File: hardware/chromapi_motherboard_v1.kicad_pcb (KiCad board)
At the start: 4 copper layers, 139 parts, among them J1 Battery Input, J10 Top Left Switch, J11 Top Right Switch, J12 Bottom Left Switch, J13 Bottom Right Switch, J14 RPI_Connector, J2 Power Switch, J3 USB_C_Receptacle_USB2.0_14P, J4 Conn_ST_STDC14, J5 Conn_TopLeft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

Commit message: rm cached
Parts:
- H2, H3, H4, H5: footprint MountingHole:MountingHole_2.7mm_M2.5_ISO14580_Pad_TopBottom -> MountingHole:MountingHole_2.7mm_M2.5_Pad_Via
- U2: footprint Package_SO:VSSOP-10_3x3mm_P0.5mm -> Package_SO:TSSOP-10_3x3mm_P0.5mm
- moved TP4 59.8 mm to (146.0, 122.0)
- moved R24 52.5 mm to (148.5, 121.3), turned to 90 degrees
- moved TP3 52.1 mm to (151.5, 122.0)
- moved D7 48.8 mm to (148.5, 124.2), turned to 90 degrees
- moved R23 45.2 mm to (154.0, 121.5), turned to 90 degrees
- moved TP2 45.2 mm to (157.5, 122.0)
- moved D6 41.8 mm to (154.0, 124.4), turned to 90 degrees
- moved R22 37.6 mm to (160.0, 121.6), turned to 90 degrees
- moved J5 37.4 mm to (186.0, 122.4), turned to 0 degrees
- moved D5 34.7 mm to (160.0, 124.5), turned to 90 degrees
- moved J7 31.2 mm to (186.0, 116.4), turned to 0 degrees
- moved J6 30.5 mm to (175.0, 122.5), turned to 0 degrees
- moved TP1 24.3 mm to (205.0, 121.5)
- moved J8 22.2 mm to (175.0, 116.4), turned to 0 degrees
- moved C5 19.1 mm to (191.5, 108.3)
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
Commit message: First routing draft
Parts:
- moved FID3 54.0 mm to (192.7, 80.7)
- moved FID2 32.2 mm to (150.0, 107.3)
- moved C36 17.7 mm to (132.2, 116.5)
- moved C37 17.7 mm to (140.7, 116.5)
- moved J11 17.5 mm to (141.5, 122.5)
- moved R33 17.5 mm to (133.5, 118.0)
- moved R34 17.5 mm to (142.0, 118.0)
- moved J10 17.5 mm to (133.0, 122.5)
- moved J12 16.5 mm to (116.0, 122.5)
- moved J13 16.5 mm to (124.5, 122.5)
- moved C39 16.5 mm to (123.7, 116.5)
- moved R35 16.5 mm to (116.5, 118.0)
- moved R36 16.5 mm to (125.0, 118.0)
- moved C38 16.3 mm to (115.2, 116.5)
- moved J8 11.1 mm to (186.1, 116.4)
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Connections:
- J14 pad 36: unconnected-(J14-Pin_36-Pad36) -> /Raspberry Pi Interface/NRST
- J14 pad 37: /Raspberry Pi Interface/NRST -> unconnected-(J14-Pin_37-Pad37)
- J2 pad 1: /Power Supply & Charge/B+ -> /Power Supply & Charge/V_BATT
- J2 pad 2: /Power Supply & Charge/V_BATT -> /Power Supply & Charge/B+
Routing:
- net +3.3V: track 0.00 -> 266.6 mm, vias 0 -> 7
- net /Raspberry Pi Interface/NRST: track 0.00 -> 96.8 mm, vias 0 -> 2
- net /STM32 Microcontroller Core/SERVO_DATA: track 0.00 -> 68.1 mm, vias 0 -> 1
- net /Peripherals (Sensors & Audio)/MIC_DOUT: track 0.00 -> 66.6 mm
- net /Peripherals (Sensors & Audio)/LRCLK: track 0.00 -> 65.6 mm, vias 0 -> 1
- net /Peripherals (Sensors & Audio)/DIN: track 0.00 -> 52.0 mm, vias 0 -> 1
- net /Peripherals (Sensors & Audio)/SW_BotLeft: track 0.00 -> 41.0 mm, vias 0 -> 2
- net /Peripherals (Sensors & Audio)/BCLK: track 0.00 -> 40.4 mm, vias 0 -> 1
- net /Peripherals (Sensors & Audio)/SW_BotRight: track 0.00 -> 38.1 mm, vias 0 -> 2
- net /Power Supply & Charge/INA226_SDA: track 0.00 -> 37.8 mm, vias 0 -> 2
- net +5V: track 0.00 -> 35.1 mm, vias 0 -> 4
- net /Peripherals (Sensors & Audio)/SW_TopRight: track 0.00 -> 32.7 mm
- net /Raspberry Pi Interface/Fan_PWM: track 0.00 -> 31.6 mm
- net /Power Supply & Charge/INA226_SCL: track 0.00 -> 31.5 mm, vias 0 -> 2
- net /STM32 Microcontroller Core/SWDIO: track 0.00 -> 30.8 mm, vias 0 -> 2
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- added copper zone on In2.Cu, net +5V
- added copper zone on F.Cu, net /Power Supply & Charge/B+
- added copper zone on In2.Cu, net /Power Supply & Charge/V_SYS
- added copper zone on B.Cu, net GND
- added copper zone on F.Cu, net GND
- added copper zone on In1.Cu, net GND
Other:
- board outline added: 105.4 x 57.9 mm

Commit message: Routing update
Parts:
- moved C21 0.99 mm to (134.3, 106.9), turned to 0 degrees
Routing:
- net +5V: track 35.1 -> 49.2 mm, vias 4 -> 7
- net +3.3V: track 266.6 -> 263.1 mm
- net GND: track 0.00 -> 2.34 mm, vias 20 -> 24
- net /STM32 Microcontroller Core/USART2_DE: track 23.9 -> 25.4 mm
- net /Peripherals (Sensors & Audio)/BCLK: track 40.4 -> 41.9 mm
- net /Peripherals (Sensors & Audio)/DIN: track 52.0 -> 52.5 mm

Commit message: Routing update
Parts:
- moved FID2 41.2 mm to (109.2, 113.0)
- moved H1 37.2 mm to (152.4, 108.3)
- moved R19 10.4 mm to (157.8, 88.0), turned to 180 degrees
- moved R21 8.17 mm to (157.7, 89.5)
- moved R15 7.66 mm to (157.5, 91.5)
- moved Q4 5.50 mm to (189.0, 89.3)
- moved L1 5.32 mm to (189.8, 97.8)
- moved C6 5.00 mm to (174.0, 91.5)
- moved D1 5.00 mm to (181.0, 89.8)
- moved U3 4.85 mm to (181.1, 99.3)
- moved C18 4.79 mm to (151.8, 117.4)
- moved C19 4.79 mm to (146.1, 117.4)
- moved U5 4.79 mm to (148.9, 117.5)
- moved TP1 4.62 mm to (200.4, 121.8)
- moved D2 4.18 mm to (173.0, 99.6)
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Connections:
- J1 pad 2: /Power Supply & Charge/BM -> /Power Supply & Charge/B-
- J1 pad 3: /Power Supply & Charge/B- -> /Power Supply & Charge/BM
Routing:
- net /Power Supply & Charge/B+: track 0.00 -> 55.8 mm, vias 0 -> 3
- net Net-(U4-VCC): track 0.00 -> 25.4 mm
- net GND: track 2.34 -> 22.9 mm, vias 24 -> 32
- net /Power Supply & Charge/V_BATT: track 0.00 -> 17.2 mm
- net Net-(C17-Pad1): track 0.00 -> 17.1 mm
- net +3.3V: track 263.1 -> 278.9 mm
- net +5V: track 49.2 -> 63.9 mm
- net /Voltage regulation/EN: track 0.00 -> 13.1 mm
- net /Power Supply & Charge/BM: track 0.00 -> 12.3 mm
- net /Power Supply & Charge/V_SYS: track 0.00 -> 11.8 mm
- net Net-(Q1-G): track 0.00 -> 11.2 mm, vias 0 -> 2
- net Net-(U1-VC): track 0.00 -> 8.25 mm
- net /Power Supply & Charge/B-: track 0.00 -> 8.10 mm
- net Net-(U3-CE): track 0.00 -> 7.77 mm
- net Net-(U4-PG): track 0.00 -> 7.52 mm
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- added copper zone on F.Cu, net /Power Supply & Charge/B-
- added copper zone on F.Cu, net Net-(C7-Pad1)
- added copper zone on F.Cu, net Net-(D1-A)
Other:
- board size 105.4 x 57.9 mm -> 105.5 x 59.4 mm
- board text added: "3.3V"
- board text added: "5V"
- board text added: "7.2V"
- board text added: "BL"
- board text added: "BR"
- board text added: "Battery"
- board text added: "BotLeft"
- board text added: "BotRight"
- board text added: "Chromapi"
- board text added: "Contact Switches"
- board text added: "Debug"
- board text added: "Fan"
- board text added: "GND"
- board text added: "IMU"
- board text added: "MIC"
- board text added: "Power Switch"
- board text added: "Servo Connectors"
- board text added: "Speaker"
- board text added: "TL"
- board text added: "TR"
- board text added: "TopLeft"
- board text added: "TopRight"

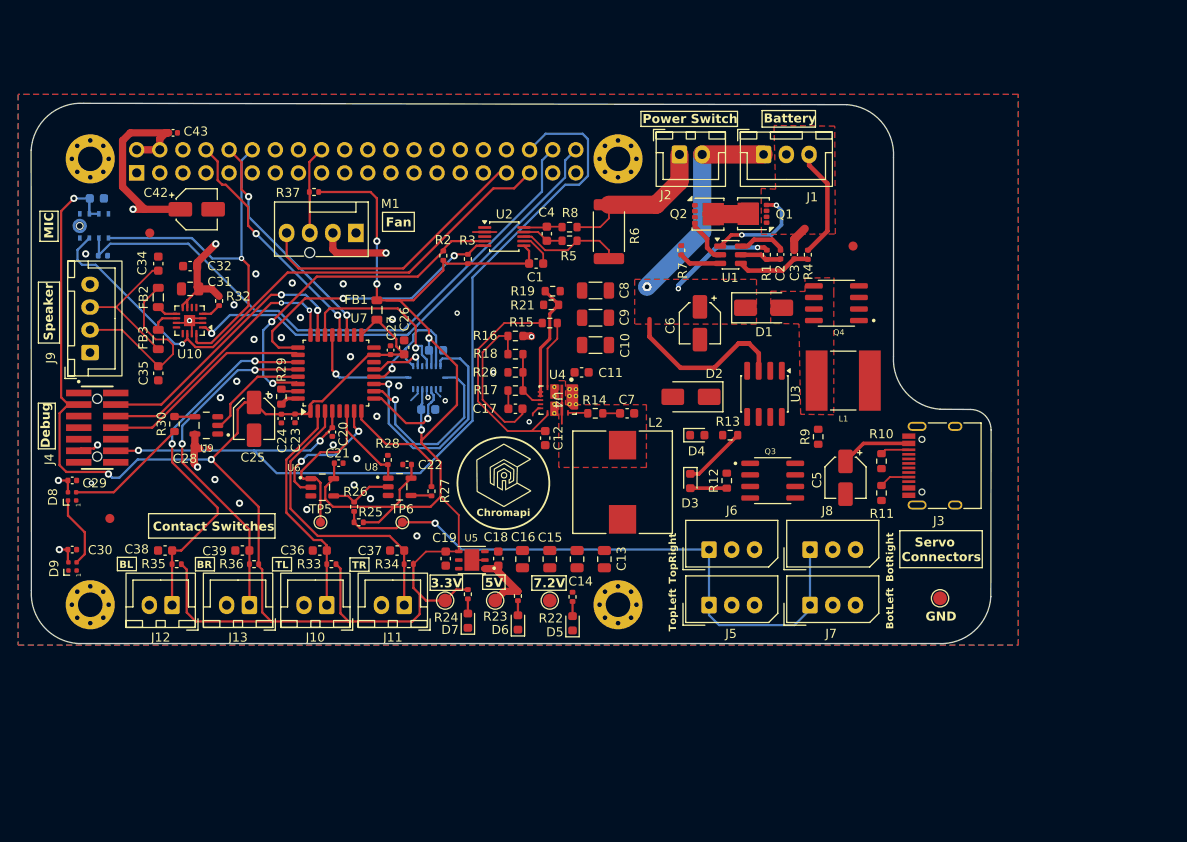
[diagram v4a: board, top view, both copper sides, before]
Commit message: Finishing first draft of routing
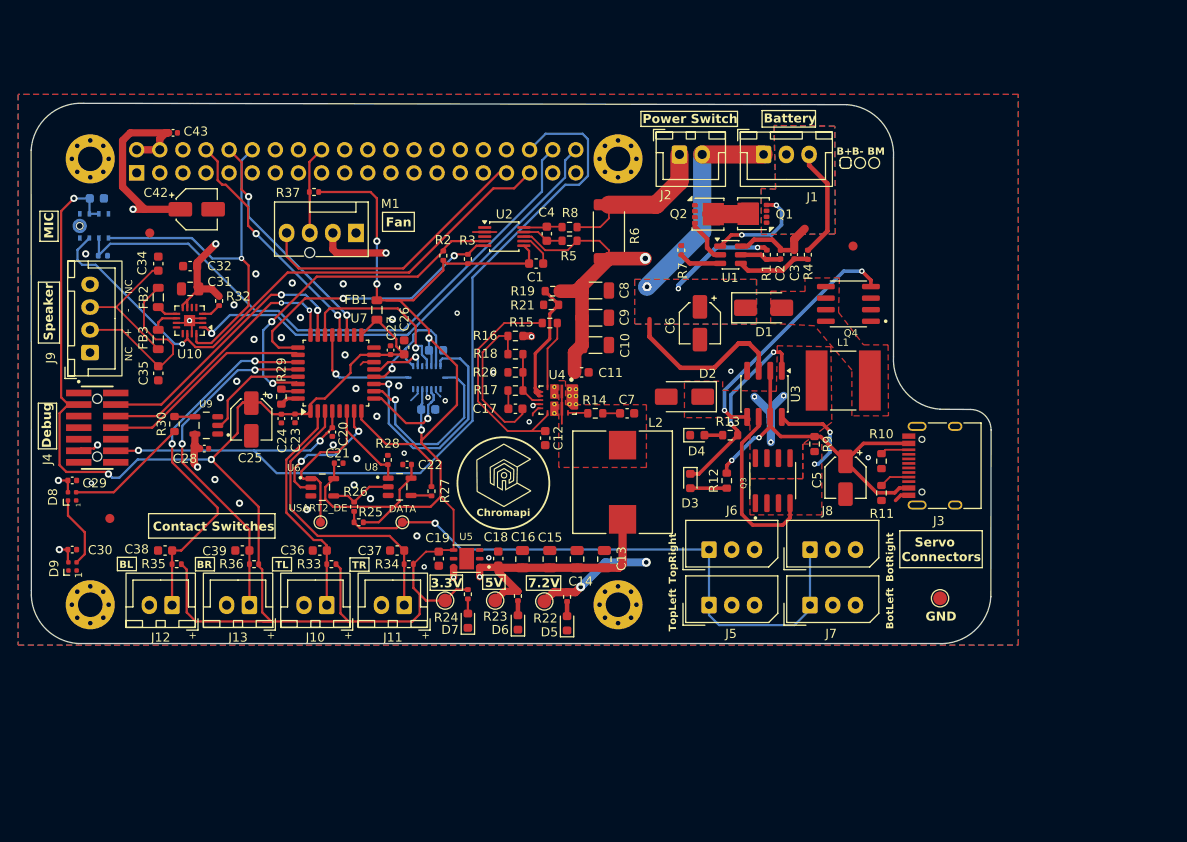
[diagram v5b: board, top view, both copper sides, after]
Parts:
- moved Q4 1.32 mm to (190.3, 89.4)
- moved R9 0.89 mm to (186.6, 104.8), turned to -90 degrees
- moved C19 0.77 mm to (145.3, 117.4)
- moved D2 0.72 mm to (172.3, 99.6)
- moved TP2 0.61 mm to (156.9, 122.1)
- moved D5 0.60 mm to (159.4, 124.5)
- moved R22 0.60 mm to (159.4, 121.6)
- moved U5 0.59 mm to (148.4, 117.4)
- moved C25 0.31 mm to (124.7, 102.1)
- turned L1 to 0 degrees
- turned Q3 to 90 degrees
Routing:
- net /Power Supply & Charge/V_SYS: track 11.8 -> 45.5 mm, vias 0 -> 3
- net Net-(U3-CE): track 7.77 -> 39.8 mm, vias 0 -> 2
- net Net-(Q4-G): track 0.00 -> 27.6 mm, vias 0 -> 2
- net +5V: track 63.9 -> 84.8 mm, vias 7 -> 10
- net Net-(U3-HDRV): track 0.00 -> 19.2 mm
- net Net-(D3-K): track 6.96 -> 21.2 mm, vias 0 -> 2
- net Net-(D2-K): track 0.00 -> 10.9 mm, vias 0 -> 3
- net Net-(U3-CSN): track 0.00 -> 10.5 mm, vias 0 -> 2
- net Net-(D4-A): track 0.00 -> 2.00 mm
- net GND: track 22.9 -> 24.7 mm, vias 32 -> 38
- net /Power Supply & Charge/B-: track 8.10 -> 9.60 mm
- net /Voltage regulation/EN: track 13.1 -> 14.3 mm
- net +3.3V: track 278.9 -> 279.5 mm
- added copper zone on B.Cu, net /Power Supply & Charge/B+
- added copper zone on B.Cu, net /Power Supply & Charge/B-
- added copper zone on F.Cu, net Net-(D2-K)
- added copper zone on F.Cu, net Net-(U3-CSN)
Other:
- board text added: "+"
- board text added: "-"
- board text added: "B+"
- board text added: "B-"
- board text added: "BM"
- board text added: "DATA"
- board text added: "NC"
- board text added: "USART2_DE"

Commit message: Solving DRC
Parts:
- U4: footprint Chromapi_FP:VAB0013A-MFG -> Chromapi_FP:TPS513885VABR
- moved C25 1.35 mm to (124.8, 103.5)
- moved D8 1.00 mm to (105.0, 111.5)
- moved R19 0.83 mm to (157.6, 87.2)
- moved C23 0.77 mm to (129.8, 102.7)
- moved C24 0.65 mm to (128.2, 102.6)
- moved C26 0.53 mm to (141.6, 93.7)
- moved R29 0.52 mm to (127.5, 99.8)
- moved R17 0.43 mm to (153.7, 99.3)
- moved FID2 0.41 mm to (109.3, 113.3)
- moved C11 0.35 mm to (161.0, 96.6)
- moved C22 0.28 mm to (142.1, 107.0)
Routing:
- net +3.3V: track 279.5 -> 276.3 mm
- net Net-(D2-K): track 10.9 -> 8.23 mm
- net GND: track 24.7 -> 22.7 mm, vias 38 -> 41
- net +5V: track 84.8 -> 86.2 mm
- net /STM32 Microcontroller Core/USART2_DE: track 25.4 -> 24.2 mm
- net /Voltage regulation/EN: track 14.3 -> 15.2 mm
- net /Power Supply & Charge/V_SYS: track 45.5 -> 46.3 mm, vias 3 -> 6
